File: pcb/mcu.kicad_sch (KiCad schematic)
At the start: 32 parts, among them J1 Conn_01x02_Pin, SW2 SW_Push, U1 TLV1117LV33DCYR, U2 W25Q64JVSSIQ_C179171, U3 STM32H750VBTx, Y1 25 MHz

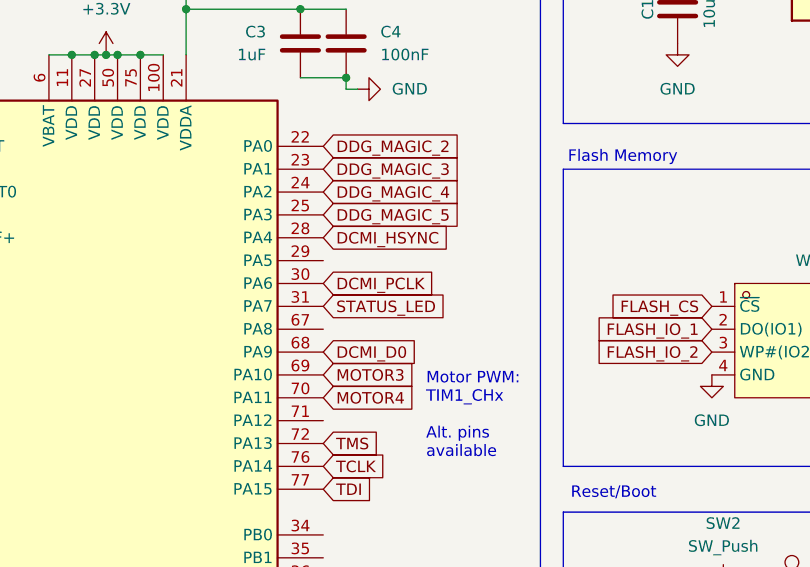
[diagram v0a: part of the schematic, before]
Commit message: [pcb] small fixes and improvements
- add two status LEDs
- move silkscreen labels for better visibility
- add more silkcreen logos/credits
- fix nrf footprint, add rf keepout zone
- add mounting holes
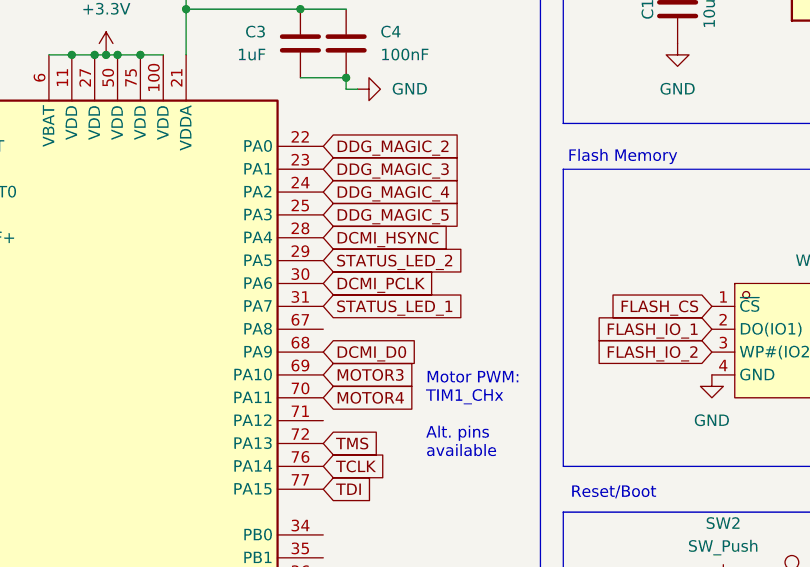
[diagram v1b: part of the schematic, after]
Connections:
- net STATUS_LED_2: now reaches U3.29 (PA5)
- net STATUS_LED renamed STATUS_LED_1
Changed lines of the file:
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@@
+		)
+	)
+	(global_label "STATUS_LED_1"
+		(shape input)
+		(at 87.63 63.5 0)
+		(fields_autoplaced yes)
+		(effects
+			(font
+				(size 1.27 1.27)
+			)
+			(justify left)
+		)
+		(property "Intersheetrefs" "${INTERSHEET_REFS}"
+			(at 103.9803 63.5 0)
+			(effects
+				(font
+					(size 1.27 1.27)
+				)
+				(justify left)
+				(hide yes)
+			)
 		)
 	)
@@
 		)
 	)
+	(global_label "STATUS_LED_2"
+		(shape input)
+		(at 87.63 58.42 0)
+		(fields_autoplaced yes)
+		(effects
+			(font
+				(size 1.27 1.27)
+			)
+			(justify left)
+		)
+		(property "Intersheetrefs" "${INTERSHEET_REFS}"
+			(at 103.9803 58.42 0)
+			(effects
+				(font
+					(size 1.27 1.27)
+				)
+				(justify left)
+				(hide yes)
+			)
+		)
+	)
 	(global_label "DDG_MAGIC_3"
 		(shape input)
@@
 				(hide yes)
 			)
-		)
-	)
-	(global_label "STATUS_LED"
-		(shape input)
-		(at 87.63 63.5 0)
-		(fields_autoplaced yes)
-		(effects
-			(font
-				(size 1.27 1.27)
-			)
-			(justify left)
-		)
-		(property "Intersheetrefs" "${INTERSHEET_REFS}"
-			(at 101.8032 63.5 0)
-			(effects
-				(font
-					(size 1.27 1.27)
-				)
-				(justify left)
-				(hide yes)
-			)

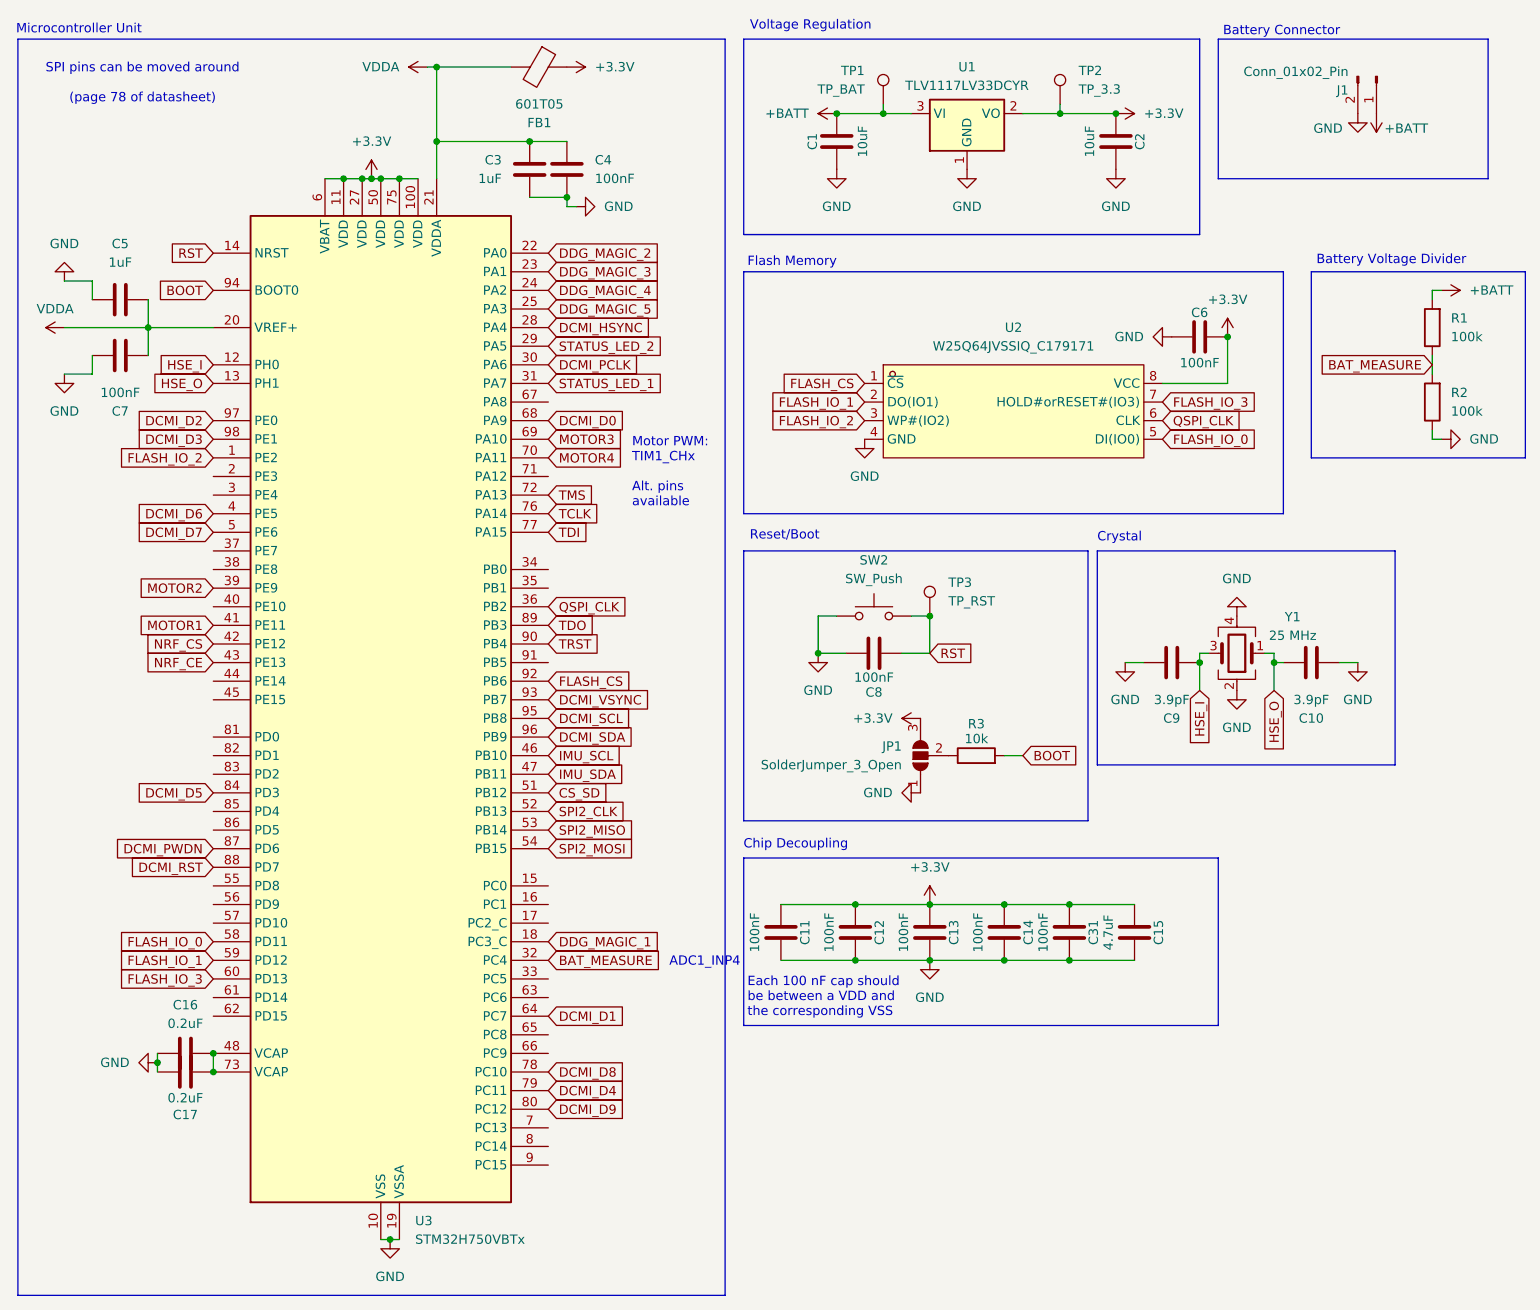
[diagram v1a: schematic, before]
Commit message: [pcb] remove on-board camera
- remove camera and all supporting components (we'll be using an external dedicated board)
- extend DDG header
- make PCB smaller
- add more silkscreen labels
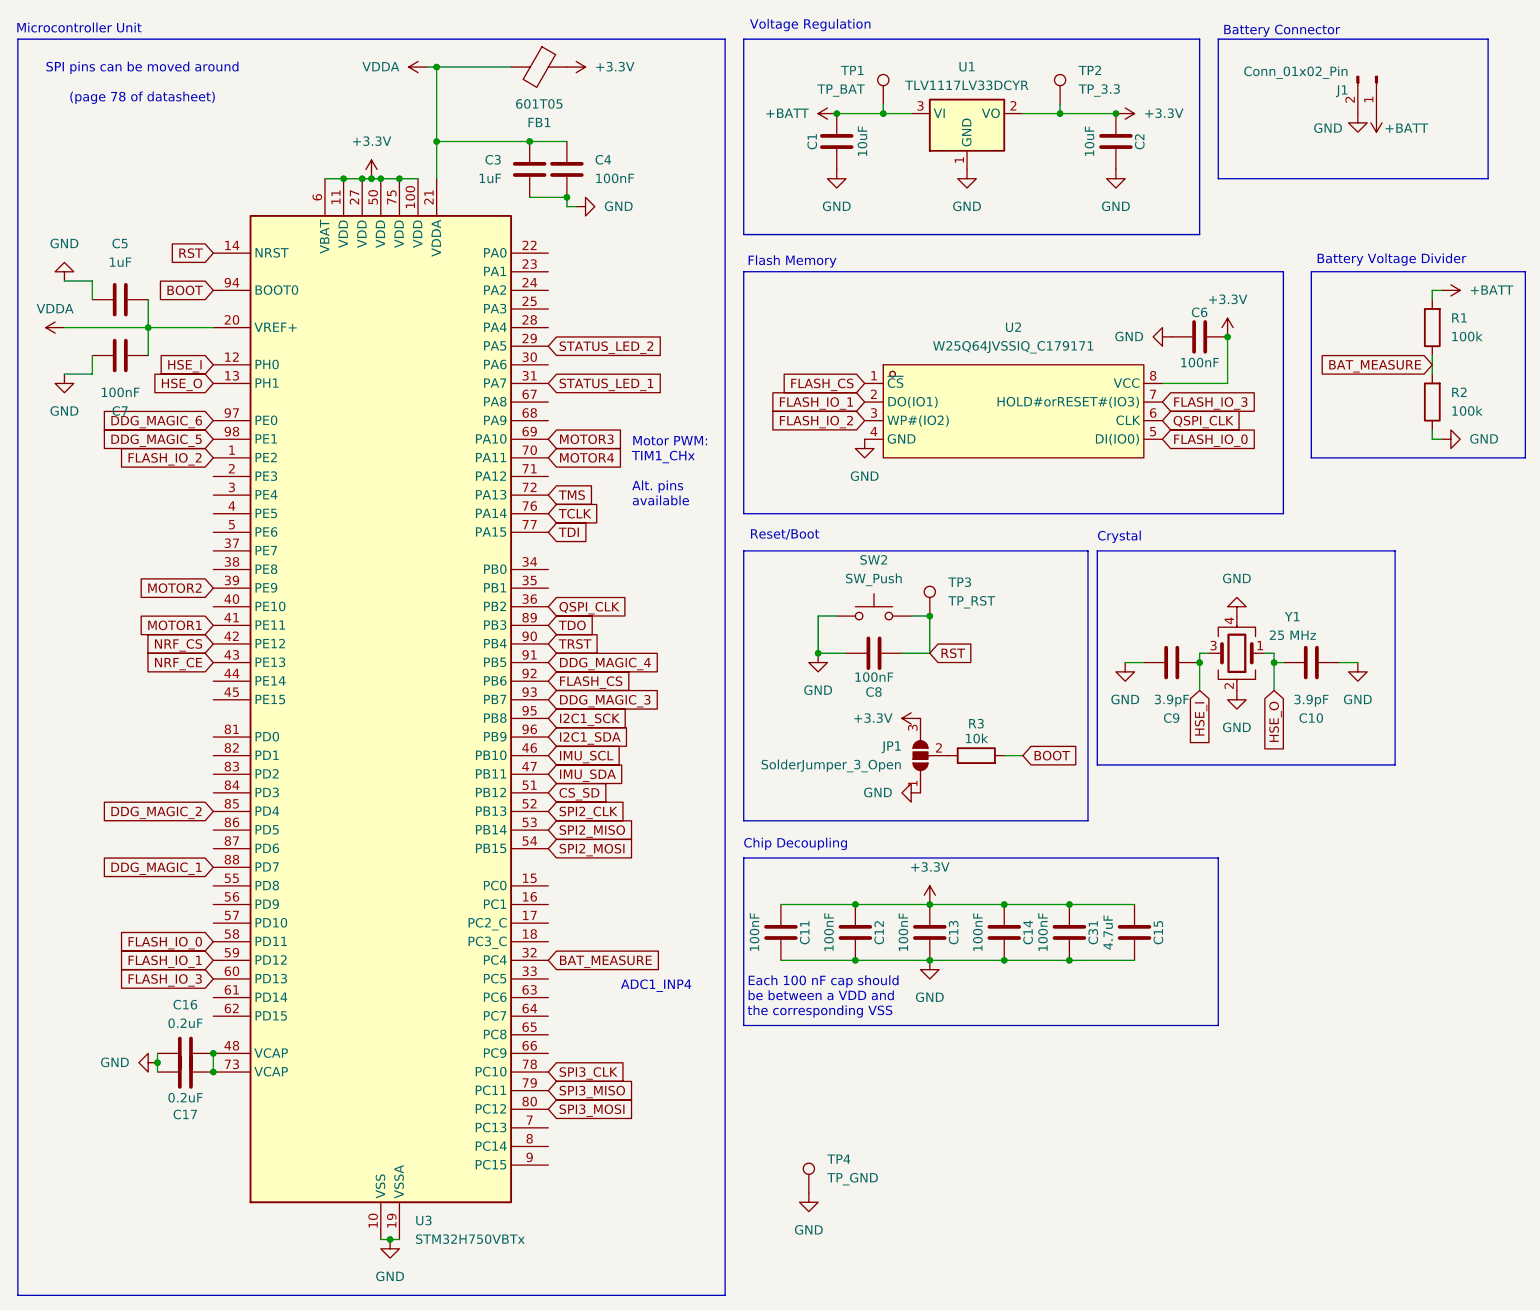
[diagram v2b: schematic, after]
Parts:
- added TP4: TP_GND, TestPoint:TestPoint_Pad_D2.0mm, symbol Connector:TestPoint
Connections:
- net DCMI_D3 is gone; now on net DDG_MAGIC_5: U3.98 (PE1)
- net DCMI_RST is gone; now on net DDG_MAGIC_1: U3.88 (PD7)
- net DCMI_VSYNC is gone; now on net DDG_MAGIC_3: U3.93 (PB7)
- net DDG_MAGIC_1: no longer U3.18 (PC3_C)
- net DDG_MAGIC_2: now also U3.85 (PD4); no longer U3.22 (PA0)
- net DDG_MAGIC_3: no longer U3.23 (PA1)
- net DDG_MAGIC_4: now also U3.91 (PB5); no longer U3.24 (PA2)
- net DDG_MAGIC_5: no longer U3.25 (PA3)
- net GND: now also TP4.1
- net DCMI_D0: no longer names the net of U3.68 (PA9)
- net DCMI_D1: no longer names the net of U3.64 (PC7)
- net DCMI_D2 renamed DDG_MAGIC_6
- net DCMI_D4 renamed SPI3_MISO
- net DCMI_D5: no longer names the net of U3.84 (PD3)
- net DCMI_D6: no longer names the net of U3.4 (PE5)
- net DCMI_D7: no longer names the net of U3.5 (PE6)
- net DCMI_D8 renamed SPI3_CLK
- net DCMI_D9 renamed SPI3_MOSI
- net DCMI_HSYNC: no longer names the net of U3.28 (PA4)
- net DCMI_PCLK: no longer names the net of U3.30 (PA6)
- net DCMI_PWDN: no longer names the net of U3.87 (PD6)
- net DCMI_SCL renamed I2C1_SCK
- net DCMI_SDA renamed I2C1_SDA
